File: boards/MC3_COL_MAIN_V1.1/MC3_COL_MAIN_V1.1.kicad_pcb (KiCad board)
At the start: 4 copper layers, 66.5 x 66.5 mm, 155 parts, among them J10 MOTOR, J12 CAN, J13 HARNESS_FFC_6P, J2 SWD, J3 ENC_leaf1, J4 ENC_leaf2, J5 ENC_leaf3, J6 ENC_leaf4, J7 MOTOR, J8 MOTOR, J9 MOTOR, Q1 AO4421, SW1 SKRKAEE020, U1 AMS1117-3.3, U10 GP1S094HCZ0F, U11 GP1S094HCZ0F, U12 LM61460AANRJRR, U2 STM32U595RJT6, U3 DRV8214RTER, U4 DRV8214RTER, U5 DRV8214RTER, U6 DRV8214RTER, U7 DRV8214RTER, U8 TJA1051T/3, U9 AEDR-8300-1Q0, Y1 8MHz

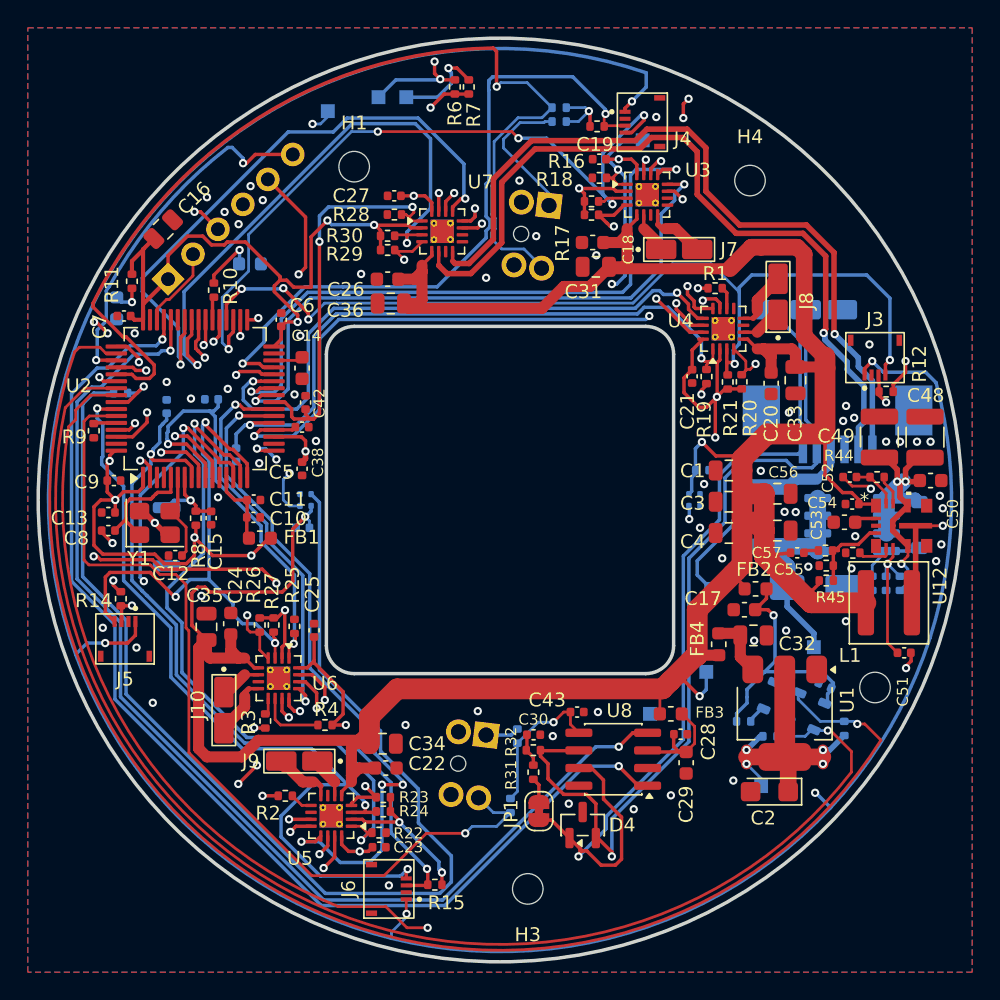
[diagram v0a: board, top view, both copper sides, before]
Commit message: V1.1 artwork: OXOS_Logo_Big on back silk; logo/slot footprints into project lib
Co-Authored-By: Claude Fable 5 <noreply@anthropic.com>
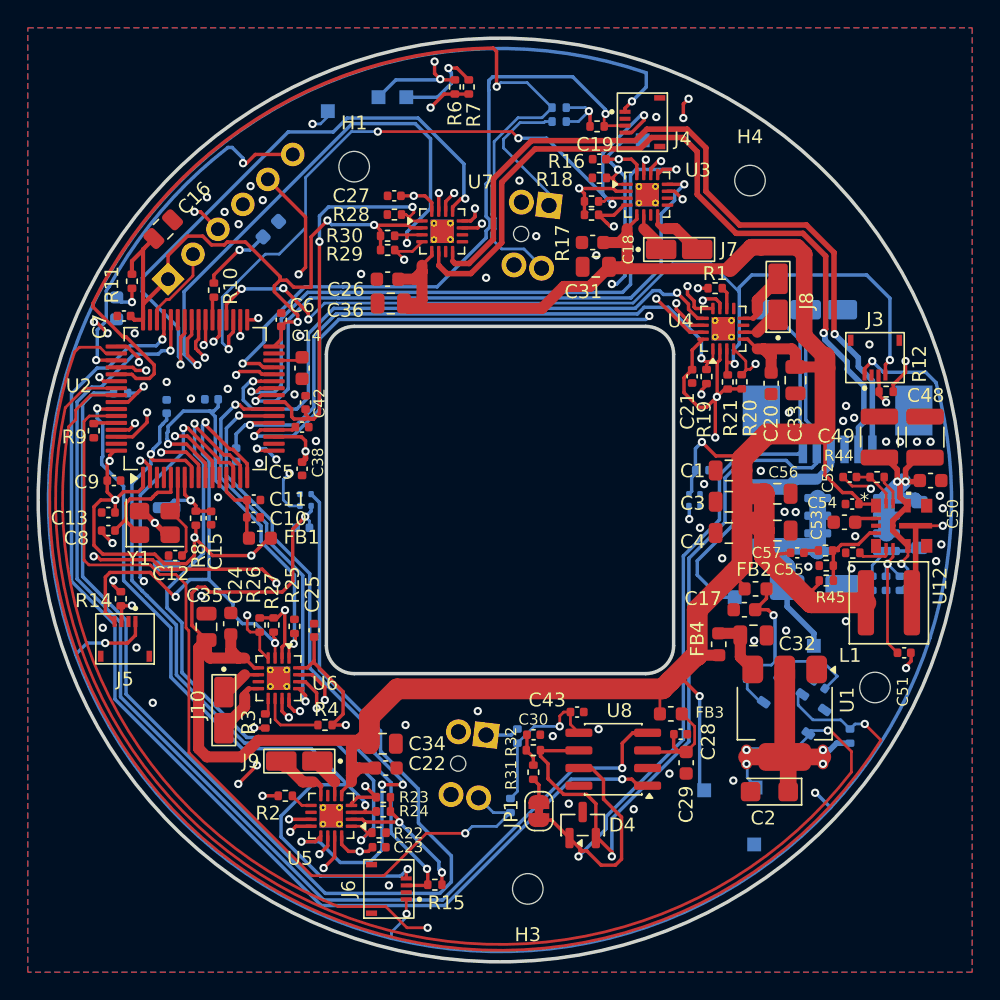
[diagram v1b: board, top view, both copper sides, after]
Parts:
- added G8: OXOS_Logo_Big, MC3_COL_MAIN:OXOS_Logo_Big, B.Cu at (117.7, 80.6)
- moved TP7 12.0 mm to (118.3, 124.8)
- moved TP1 8.53 mm to (114.7, 120.9)
- moved R33 3.55 mm to (117.8, 112.4), turned to -90 degrees
- moved D2 2.92 mm to (83.5, 80.5), turned to -135 degrees
- moved TP9 1.80 mm to (116.9, 107.0)
- moved R35 1.05 mm to (119.8, 118.0)
- moved R34 0.69 mm to (125.2, 117.0)
- moved TP3 0.41 mm to (118.4, 120.7)
- moved C37 0.41 mm to (123.0, 113.3), turned to 145 degrees
- moved TP2 0.10 mm to (122.6, 110.5)
- turned U9 to 145 degrees
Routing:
- net VM: track 215.4 -> 220.4 mm
- net VSENS: track 54.0 -> 49.9 mm
- net VIN_PAD: track 16.1 -> 18.0 mm
- net CAN1_RX: track 82.0 -> 83.1 mm
- net Net-(U9-VLED): track 1.28 -> 2.27 mm
- net CAN1_TX: track 82.2 -> 81.4 mm
- net /MCU/LED_HB_A: track 4.54 -> 5.26 mm
- net RC_OUT_leaf1: track 55.9 -> 56.5 mm
- net /MCU/YAW_ENC_A: track 11.0 -> 11.6 mm
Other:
- board text added: "MC3 COL MK1"

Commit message: V1.1: LQFP-64 pads 0.30->0.26 (0.24mm mask dams for matte black), J13 courtyard to closed-body edge, J13 radial rotation; F8 value sync
Co-Authored-By: Claude Fable 5 <noreply@anthropic.com>
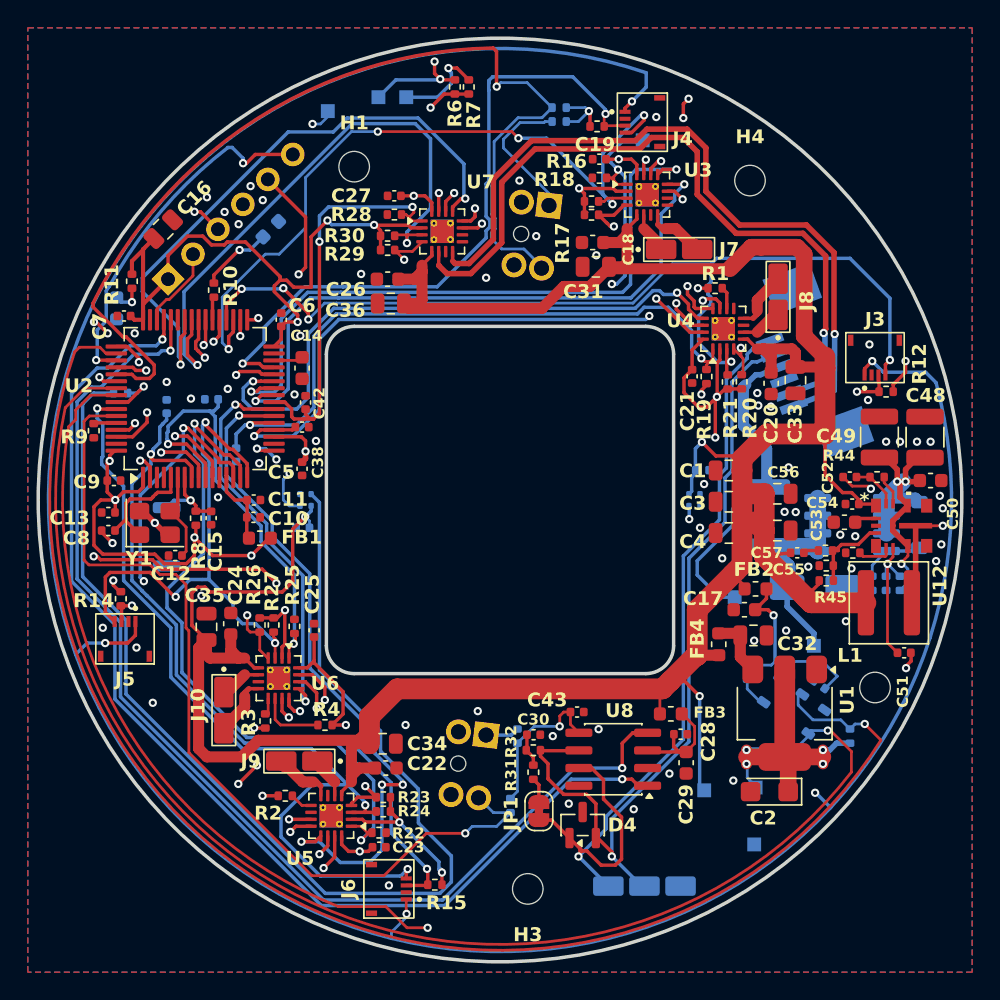
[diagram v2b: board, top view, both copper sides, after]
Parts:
- J3: value ENC_leaf1 -> ENC_leaf2
- J4: value ENC_leaf2 -> ENC_leaf1
- J5: value ENC_leaf3 -> ENC_leaf4
- J6: value ENC_leaf4 -> ENC_leaf3
- moved G8 49.7 mm to (83.9, 117.0)
- moved J12 43.1 mm to (110.4, 127.8)
- moved J13 4.86 mm to (122.0, 90.3), turned to -70 degrees
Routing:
- net VIN_PAD: track 18.0 -> 23.2 mm
- net CANL: track 63.8 -> 59.1 mm
- net YAW_OUT1: track 57.0 -> 52.8 mm
- net CANH: track 66.1 -> 62.8 mm
- net RC_OUT_leaf2: track 68.0 -> 71.0 mm
- net ENC_leaf2: track 82.2 -> 79.7 mm
- net I2C1_SDA: track 100.1 -> 102.4 mm
- net YAW_OUT2: track 55.6 -> 53.4 mm
- net I2C1_SCL: track 102.0 -> 104.2 mm
- net nFAULT_leaf2: track 67.8 -> 66.2 mm
- net DRV_nSLEEP: track 138.0 -> 136.8 mm
- net GND: vias 62 -> 63

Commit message: V1.1: footprint updates applied to board (LQFP 0.26 pads, J13 courtyard, opto reroute); buck corner silk removed
Co-Authored-By: Claude Fable 5 <noreply@anthropic.com>
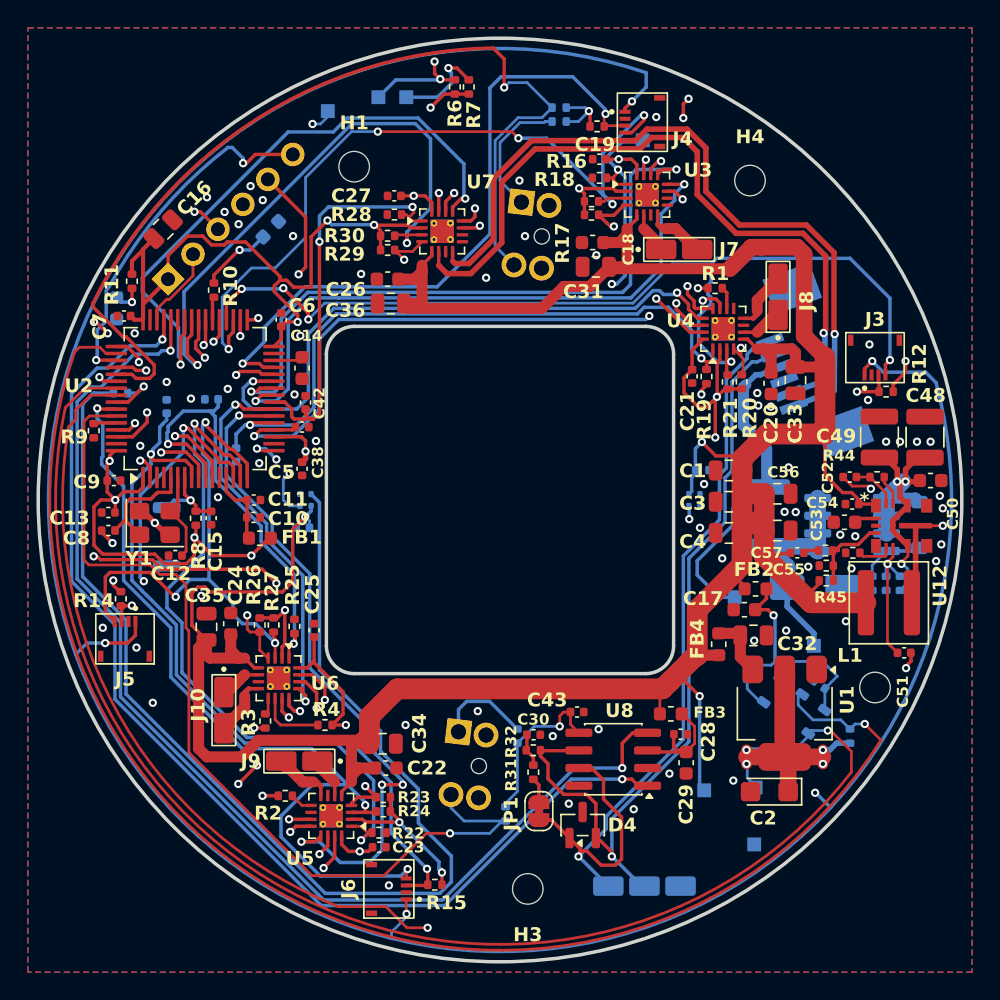
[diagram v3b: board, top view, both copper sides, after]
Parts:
- G8: value OXOS_Logo_Big -> LOGO
- moved R37 0.69 mm to (100.4, 122.6)
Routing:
- net Net-(U10-A): track 2.43 -> 6.91 mm
- net /MCU/YAW_LIM: track 35.1 -> 32.1 mm
- net /MCU/YAW_HOME: track 64.2 -> 66.1 mm
- net VSENS: track 49.9 -> 51.4 mm
- net Net-(U11-A): track 10.2 -> 9.30 mm
- net +3V3: track 213.3 -> 214.0 mm
- net ENC_leaf1: track 48.2 -> 47.6 mm
- net GND: track 5.20 -> 5.63 mm, vias 63 -> 64
